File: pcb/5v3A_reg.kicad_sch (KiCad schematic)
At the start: 7 parts, among them U2 ADP2303ARDZ-5.0

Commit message: Finished layout
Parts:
- L1: LCSC C2847561 -> C497878
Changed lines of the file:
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@@
       (effects (font (size 1.27 1.27)) hide)
     )
-    (property "LCSC" "C2847561" (id 4) (at 173.99 74.93 0)
+    (property "LCSC" "C497878" (id 4) (at 173.99 74.93 0)
       (effects (font (size 1.27 1.27)) hide)
     )

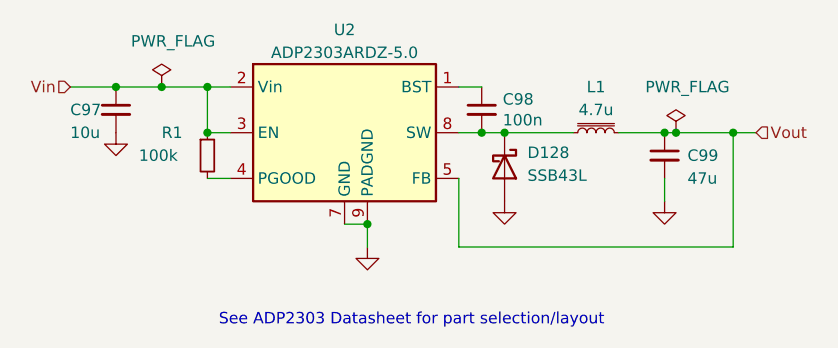
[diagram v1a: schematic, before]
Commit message: change to kicad 7, fix led signal direction for segment displays
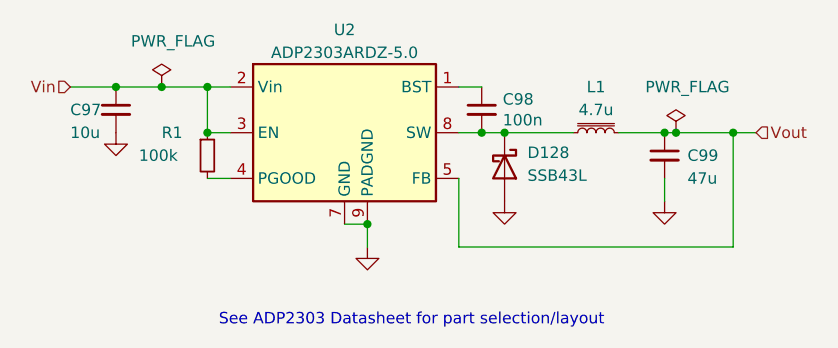
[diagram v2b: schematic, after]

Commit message: Fix kikad 7 schematic issues
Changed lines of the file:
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@@
   (junction (at 181.61 74.93) (diameter 0) (color 0 0 0 0)
   )
-  (junction (at 125.73 69.85) (diameter 0) (color 0 0 0 0)
-  )
   (junction (at 120.65 69.85) (diameter 0) (color 0 0 0 0)
-  )
-  (wire (pts (xy 125.73 69.85) (xy 130.81 69.85))
-    (stroke (width 0) (type default))
   )
   (wire (pts (xy 161.29 74.93) (xy 163.83 74.93))
@@
     (stroke (width 0) (type default))
   )
-  (wire (pts (xy 120.65 69.85) (xy 125.73 69.85))
-    (stroke (width 0) (type default))
-  )
   (wire (pts (xy 181.61 82.55) (xy 181.61 80.01))
     (stroke (width 0) (type default))
@@
   )
   (wire (pts (xy 181.61 74.93) (xy 182.88 74.93))
+    (stroke (width 0) (type default))
+  )
+  (wire (pts (xy 120.65 69.85) (xy 130.81 69.85))
     (stroke (width 0) (type default))
   )
@@
         )
       )
-    )
-  )
-  (symbol (lib_id "power:PWR_FLAG") (at 125.73 69.85 0) (unit 1)
-    (in_bom yes) (on_board yes) (dnp no)
-    (property "Reference" "#FLG0103" (at 125.73 67.945 0)
-      (effects (font (size 1.27 1.27)) hide)
-    )
-    (property "Value" "PWR_FLAG" (at 127 64.77 0)
-      (effects (font (size 1.27 1.27)))
-    )
-    (property "Footprint" "" (at 125.73 69.85 0)
-      (effects (font (size 1.27 1.27)) hide)
-    )
-    (property "Datasheet" "~" (at 125.73 69.85 0)
-      (effects (font (size 1.27 1.27)) hide)
-    )
-    (pin "1")
-    (instances
-      (project "PCB"
-        (path "/68f34db6-b185-48e2-8817-fb07f7d1240e/785c2b5b-0f6e-472e-8e4b-b02b70d5cf35/f73c095e-19b5-4ca2-82b2-71d1369b65a4"
-          (reference "#FLG0103") (unit 1)
-        )
-        (path "/68f34db6-b185-48e2-8817-fb07f7d1240e/785c2b5b-0f6e-472e-8e4b-b02b70d5cf35/bb437566-7d32-450d-b77e-65f68738184c"
-          (reference "#FLG0105") (unit 1)
-        )
-      )
